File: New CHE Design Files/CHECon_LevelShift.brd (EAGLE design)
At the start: 81.7 x 51.7 mm, 42 parts, among them U2 MAX232SOIC16, U3 RS485SOIC

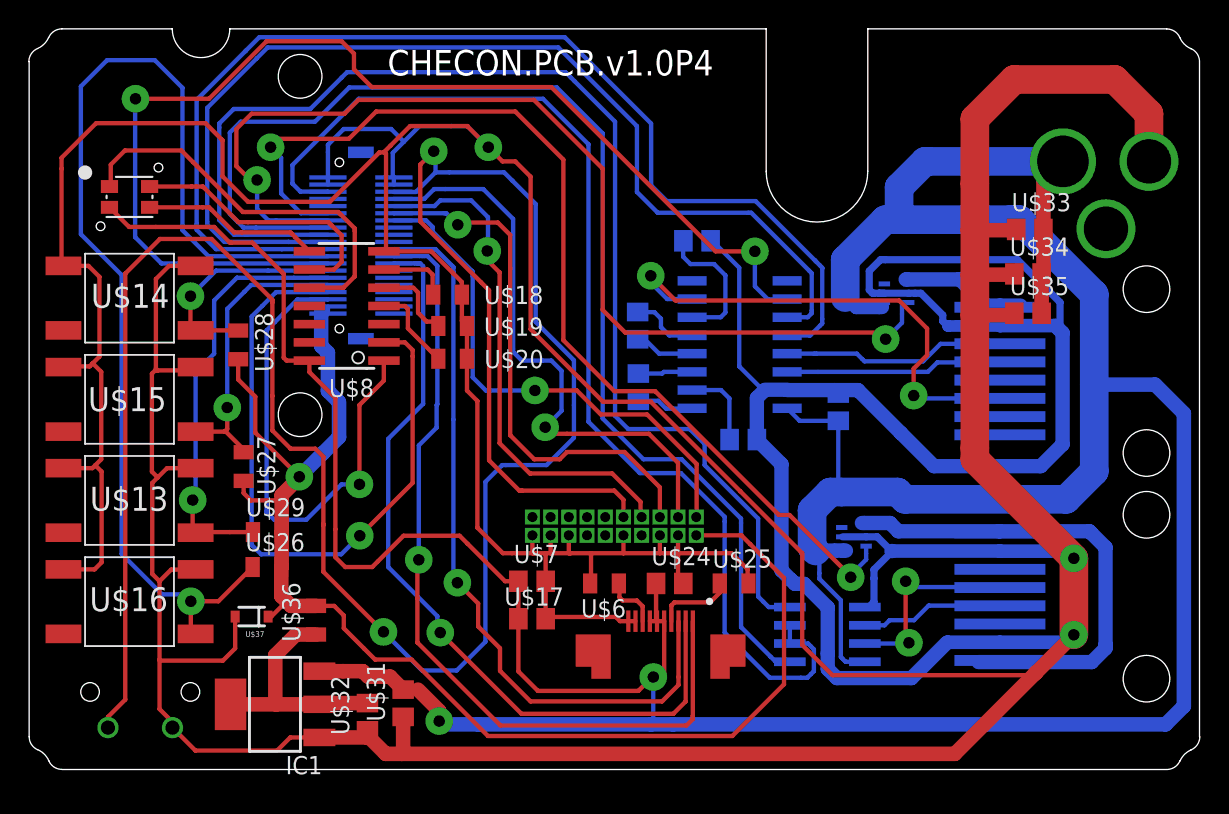
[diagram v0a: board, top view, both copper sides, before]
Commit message: P3
Added VR and Zener just in case
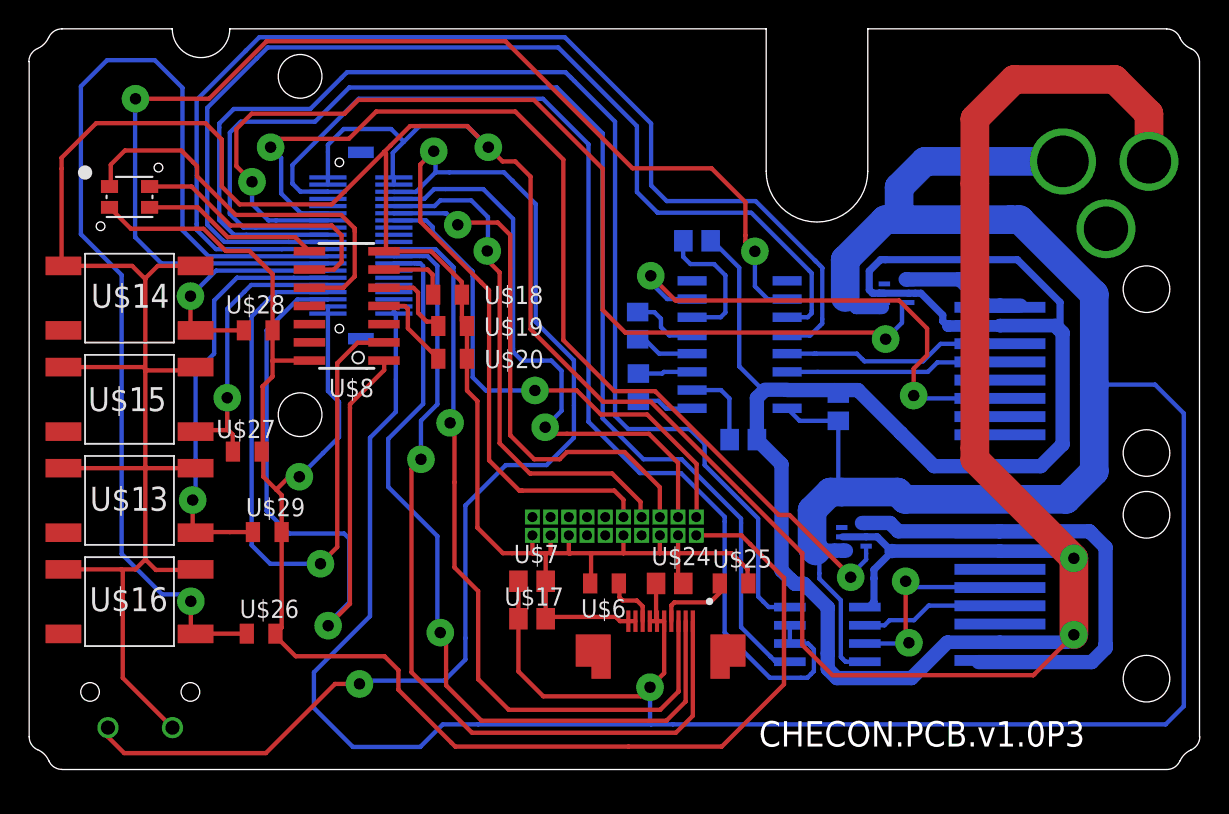
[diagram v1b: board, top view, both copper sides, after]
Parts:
- removed IC1: (no value), KW2:SOT223
- removed U$31, U$32, U$33, U$34, U$35: (no value), GW-devices:C0805
- removed U$36: (no value), GW-devices:RF-C0805
- removed U$37: DIODE-ZENER-BZT52, SparkFun:SOD-323
- moved U$26 4.67 mm to (-24.6, -16.4)
- moved U$28 1.73 mm to (-24.8, 4.80), turned to 0 degrees
- moved U$27 1.07 mm to (-25.6, -3.66), turned to 0 degrees
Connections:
- removed net OUT1: IC1.2, IC1.4, U$32.2, U$36.1
- net +3V3: now also U$1.P$2, U$8.14; no longer U$36.2, U$37.1
- net GND: no longer IC1.1, U$31.1, U$32.1, U$33.1, U$34.1, U$35.1, U$37.2
- net V+: now also U$10.P$38, U$10.P$40; no longer IC1.3, U$1.P$2, U$31.2, U$33.2, U$34.2, U$35.2, U$8.14
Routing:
- net GND: track 562.2 -> 474.8 mm
- net N$6: track 167.0 -> 115.1 mm
- net V+: track 281.2 -> 249.6 mm, vias 2 -> 1
- net +3V3: track 93.9 -> 113.7 mm
- net OUT1: track 16.4 -> 0.00 mm
- net N$11: track 34.9 -> 51.1 mm
- net N$29: track 55.6 -> 57.9 mm
- net N$31: track 52.5 -> 54.6 mm
- net N$30: track 58.8 -> 60.9 mm
- net N$34: track 78.2 -> 76.2 mm
- net N$16: track 47.1 -> 45.7 mm
- net N$41: track 80.5 -> 81.5 mm
- net N$36: track 15.8 -> 16.4 mm
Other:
- board text added: "CHECON.PCB.v1.0P3"
- board text added: "P3: Adjusted traces to use 0.4mm tool, need to add level shifter"
- board text removed: "CHECON.PCB.v1.0P4"
